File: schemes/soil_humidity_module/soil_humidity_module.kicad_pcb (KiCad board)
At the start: 2 copper layers, 9 parts, among them Q1 IRL540N, Q2 BC547, U1 nRF24L01P, U2 SEN0193

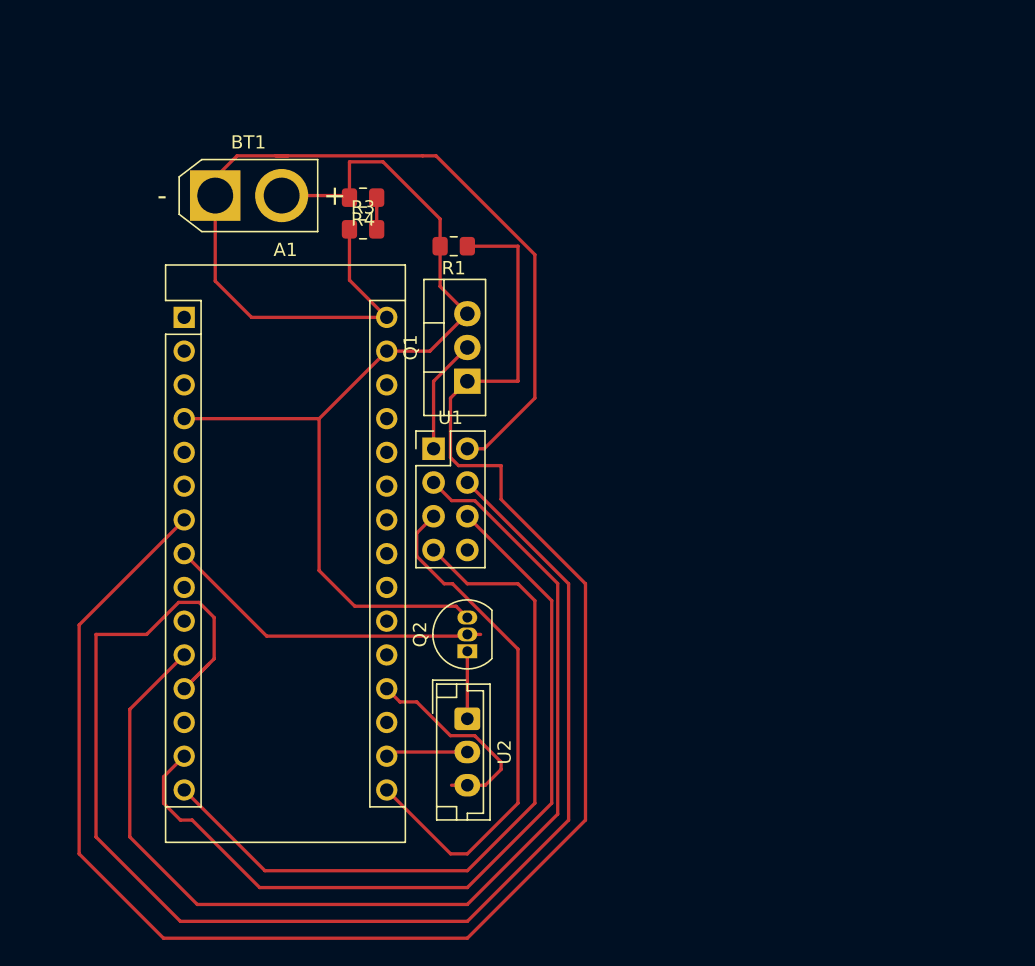
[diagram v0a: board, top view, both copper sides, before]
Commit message: [soil_huimidity_transmitter] Scheme improved. New PCB ordered
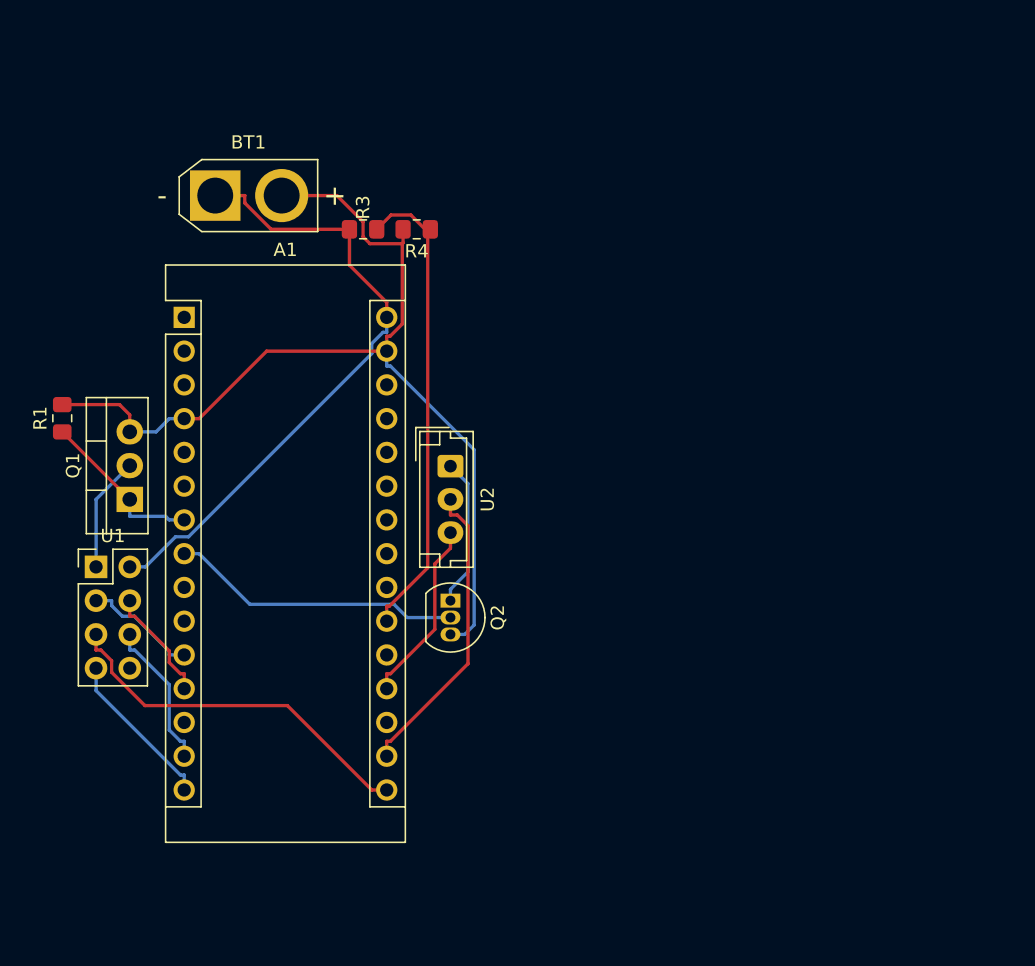
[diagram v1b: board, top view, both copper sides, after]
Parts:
- moved R1 32.2 mm to (104.1, 113.3), turned to 90 degrees
- moved Q1 26.9 mm to (109.2, 119.4)
- moved U1 26.9 mm to (106.7, 124.5)
- moved U2 19.1 mm to (133.3, 116.9)
- moved R4 4.69 mm to (130.8, 99.1)
- moved Q2 4.02 mm to (133.3, 127.0), turned to 270 degrees
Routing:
- net Net-(A1-Pad7): track 130.2 -> 12.7 mm
- net CSN: track 104.4 -> 8.70 mm
- net CE: track 82.3 -> 8.71 mm
- net MOSI: track 62.9 -> 11.2 mm
- net MISO: track 55.4 -> 12.1 mm
- net Net-(A1-Pad21): track 3.08 -> 35.8 mm
- net Net-(A1-Pad30): track 76.1 -> 47.5 mm
- net Net-(A1-Pad17): track 6.20 -> 22.9 mm
- net SCK: track 39.1 -> 27.9 mm
- net Net-(Q2-Pad1): track 5.08 -> 11.2 mm
- net Q2_B: track 24.9 -> 22.0 mm
- net Net-(A1-Pad29): track 73.1 -> 75.2 mm
- net SEN_A0: track 15.7 -> 13.9 mm
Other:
- rule trace_min: 0.2 -> 0.15
- rule via_min_size: 0.4 -> 0.7

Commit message: [soil_humidity_transmitter] Simplification of the circuit
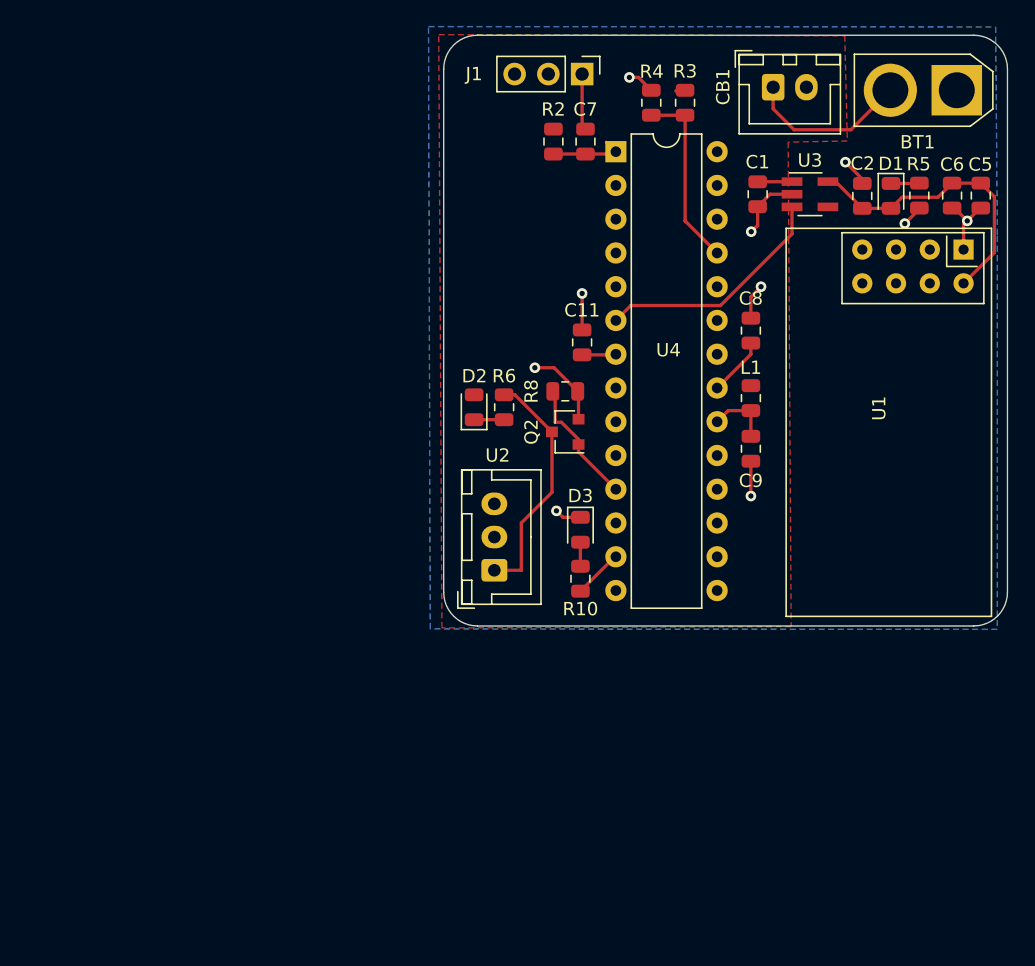
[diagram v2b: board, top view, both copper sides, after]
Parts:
- removed A1: Arduino_Nano_v3.x, Module:Arduino_Nano
- removed Q1: IRL540N, Package_TO_SOT_THT:TO-220-3_Vertical
- removed R1: 1M, Resistor_SMD:R_0805_2012Metric_Pad1.15x1.40mm_HandSolder
- added C1: 1uF, Capacitor_SMD:C_0805_2012Metric, F.Cu at (156.5, 96.4)
- added C11: 100nF, Capacitor_SMD:C_0805_2012Metric, F.Cu at (143.3, 107.6)
- added C2: 1uF, Capacitor_SMD:C_0805_2012Metric, F.Cu at (164.3, 96.5)
- added C5: 10uF, Capacitor_SMD:C_0805_2012Metric, F.Cu at (173.3, 96.5)
- added C6: 100nF, Capacitor_SMD:C_0805_2012Metric, F.Cu at (171.1, 96.5)
- added C7: 100nF, Capacitor_SMD:C_0805_2012Metric, F.Cu at (143.5, 92.5)
- added C8: 100nF, Capacitor_SMD:C_0805_2012Metric, F.Cu at (156.0, 106.7)
- added C9: 100nF, Capacitor_SMD:C_0805_2012Metric, F.Cu at (156.0, 115.6)
- added CB1: Power_Switch, Connector_JST:JST_XH_B2B-XH-A_1x02_P2.50mm_Vertical, F.Cu at (157.6, 88.4)
- added D1: LED_ALT, LED_SMD:LED_0805_2012Metric, F.Cu at (166.5, 96.5)
- added D2: LED_ALT, LED_SMD:LED_0805_2012Metric, F.Cu at (135.1, 112.4)
- added D3: LED_ALT, LED_SMD:LED_0805_2012Metric, F.Cu at (143.1, 121.7)
- added J1: Conn_01x03, Connector_PinHeader_2.54mm:PinHeader_1x03_P2.54mm_Vertical, F.Cu at (143.3, 87.4)
- added L1: 10uH, Inductor_SMD:L_0805_2012Metric, F.Cu at (156.0, 111.8)
- added R10: 1k, Resistor_SMD:R_0805_2012Metric, F.Cu at (143.1, 125.3)
- added R2: 10k, Resistor_SMD:R_0805_2012Metric, F.Cu at (141.1, 92.5)
- added R5: 1k, Resistor_SMD:R_0805_2012Metric, F.Cu at (168.6, 96.5)
- added R6: 1k, Resistor_SMD:R_0805_2012Metric, F.Cu at (137.4, 112.4)
- added R8: 1M, Resistor_SMD:R_0805_2012Metric, F.Cu at (142.0, 111.3)
- added U3: AP7365, Package_TO_SOT_SMD:SOT-23-5_HandSoldering, F.Cu at (160.4, 96.4)
- added U4: ATmega328P-PU, Package_DIP:DIP-28_W7.62mm, F.Cu at (145.8, 93.2)
- BT1: value Battery -> +3.3-4.2V
- Q2: value BC547 -> DMG6968U; footprint Package_TO_SOT_THT:TO-92_Inline -> Package_TO_SOT_SMD:SOT-23
- R3, R4: footprint Resistor_SMD:R_0805_2012Metric_Pad1.15x1.40mm_HandSolder -> Resistor_SMD:R_0805_2012Metric
- U1: value nRF24L01P -> NRF24L01_Breakout; footprint Connector_PinHeader_2.54mm:PinHeader_2x04_P2.54mm_Vertical -> RF_Module:nRF24L01_Breakout
- U2: footprint Connector_JST:JST_EH_B3B-EH-A_1x03_P2.50mm_Vertical -> Connector_JST:JST_XH_B3B-XH-A_1x03_P2.50mm_Vertical
- moved U1 69.5 mm to (172.0, 100.6), turned to 270 degrees
- moved BT1 56.4 mm to (171.4, 88.6), turned to 180 degrees
- moved R3 26.0 mm to (151.0, 89.5), turned to 270 degrees
- moved R4 20.1 mm to (148.5, 89.5), turned to 90 degrees
- moved Q2 15.4 mm to (142.0, 114.3), turned to 180 degrees
- moved U2 8.50 mm to (136.7, 124.7), turned to 90 degrees
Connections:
- net Net-(A1-Pad21) renamed DIV_A2
- BT1 pad 1: Net-(A1-Pad30) -> GND
- BT1 pad 2: Net-(A1-Pad29) -> Net-(BT1-Pad1)
- Q2 pad 1: Net-(Q2-Pad1) -> Q2_D5
- Q2 pad 2: Q2_B -> GND
- Q2 pad 3: Net-(A1-Pad29) -> Net-(Q2-Pad3)
- R3 pad 1: Net-(A1-Pad30) -> VCC
- R4 pad 2: Net-(A1-Pad29) -> GND
- U1 pad 1: CE -> GND
- U1 pad 2: CSN -> +3V3
- U1 pad 3: SCK -> CE
- U1 pad 4: MOSI -> CSN
- U1 pad 5: MISO -> SCK
- U1 pad 7: Net-(A1-Pad30) -> MISO
- U2 pad 1: Net-(Q2-Pad1) -> Net-(Q2-Pad3)
- U2 pad 2: Net-(A1-Pad17) -> VCC
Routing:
- net Net-(A1-Pad29): track 75.2 -> 0.00 mm
- net Net-(A1-Pad30): track 47.5 -> 0.00 mm
- net GND: track 0.00 -> 33.6 mm, vias 0 -> 10
- net CE: track 8.71 -> 36.8 mm
- net Net-(A1-Pad17): track 22.9 -> 0.00 mm
- net +3V3: track 0.00 -> 22.1 mm
- net Q2_B: track 22.0 -> 0.00 mm
- net DIV_A2: track 35.8 -> 13.9 mm
- net CSN: track 8.70 -> 29.9 mm
- net Net-(Q2-Pad3): track 0.00 -> 18.2 mm
- net Q1_D4: track 0.00 -> 18.0 mm
- net TXD_J1: track 0.00 -> 14.1 mm
- net MOSI: track 11.2 -> 24.0 mm
- net Net-(A1-Pad7): track 12.7 -> 0.00 mm
- net Net-(BT1-Pad1): track 0.00 -> 12.3 mm
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- added copper zone on B.Cu, net GND
- added copper zone on F.Cu, net VCC
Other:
- board outline added: 42.4 x 44.5 mm
- copper layers 2 -> 4
- rule pad_to_mask_clearance: 0.05 -> 0
- rule trace_min: 0.15 -> 0.2
- rule via_min_size: 0.7 -> 0.4
